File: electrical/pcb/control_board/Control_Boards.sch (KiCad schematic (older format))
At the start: 6 parts, among them M1 Mounting_Holes, y1 rover_silkscreen

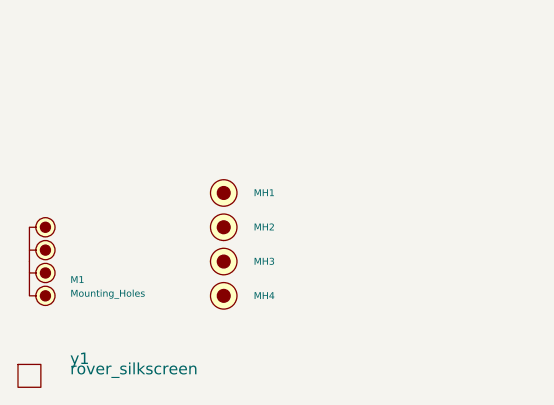
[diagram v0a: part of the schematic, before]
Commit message: moving mounting holes, unnumbering inter board connectors, and adding to kicad readme
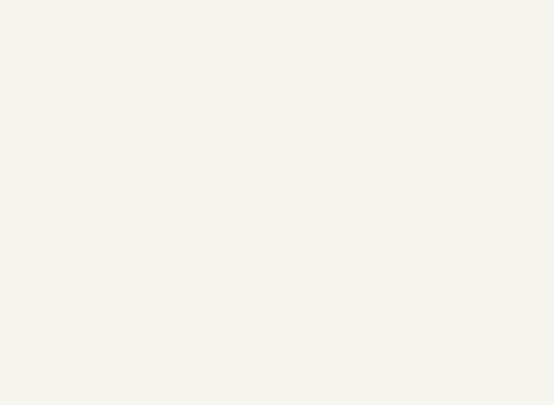
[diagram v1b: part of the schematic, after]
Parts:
- removed M1: Mounting_Holes, JPL Robotics:Raspberry pi footprint, symbol JPL_Robotics_Lib:Mounting_Holes
- removed MH1, MH2, MH3, MH4: #6THRU-HOLE, JPL Robotics:#6THRU-HOLE, symbol JPL_Robotics_Lib:#6THRU-HOLE
- removed y1: rover_silkscreen, JPL Robotics:rover_image, symbol JPL_Robotics_Lib:rover_silkscreen
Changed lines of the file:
@@
 Comment4 ""
 $EndDescr
-$Comp
-L JPL_Robotics_Lib:Mounting_Holes M1
-U 1 1 5C8D5DB2
-P 750 10200
-F 0 "M1" V 1180 10379 30  0000 L CNN
-F 1 "Mounting_Holes" V 1240 10379 30  0000 L CNN
-F 2 "JPL Robotics:Raspberry pi footprint" H 930 10380 30  0001 C CNN
-F 3 "" H 930 10380 30  0001 C CNN
-	1    750  10200
-	0    1    1    0
-$EndComp
-$Comp
-L JPL_Robotics_Lib:#6THRU-HOLE MH1
-U 1 1 5C29B1A8
-P 1600 10250
-F 0 "MH1" H 1731 10250 30  0000 L CNN
-F 1 "#6THRU-HOLE" H 1600 10390 30  0001 C CNN
-F 2 "JPL Robotics:#6THRU-HOLE" H 1600 10340 30  0001 C CNN
-F 3 "" H 1600 10340 30  0001 C CNN
-	1    1600 10250
-	1    0    0    -1
-$EndComp
-$Comp
-L JPL_Robotics_Lib:#6THRU-HOLE MH2
-U 1 1 5C29B335
-P 1600 10400
-F 0 "MH2" H 1731 10400 30  0000 L CNN
-F 1 "#6THRU-HOLE" H 1600 10540 30  0001 C CNN
-F 2 "JPL Robotics:#6THRU-HOLE" H 1600 10490 30  0001 C CNN
-F 3 "" H 1600 10490 30  0001 C CNN
-	1    1600 10400
-	1    0    0    -1
-$EndComp
-$Comp
-L JPL_Robotics_Lib:#6THRU-HOLE MH3
-U 1 1 5C2C0841
-P 1600 10550
-F 0 "MH3" H 1731 10550 30  0000 L CNN
-F 1 "#6THRU-HOLE" H 1600 10690 30  0001 C CNN
-F 2 "JPL Robotics:#6THRU-HOLE" H 1600 10640 30  0001 C CNN
-F 3 "" H 1600 10640 30  0001 C CNN
-	1    1600 10550
-	1    0    0    -1
-$EndComp
-$Comp
-L JPL_Robotics_Lib:#6THRU-HOLE MH4
-U 1 1 5C2E5D4E
-P 1600 10700
-F 0 "MH4" H 1731 10700 30  0000 L CNN
-F 1 "#6THRU-HOLE" H 1600 10840 30  0001 C CNN
-F 2 "JPL Robotics:#6THRU-HOLE" H 1600 10790 30  0001 C CNN
-F 3 "" H 1600 10790 30  0001 C CNN
-	1    1600 10700
-	1    0    0    -1
-$EndComp
-$Comp
-L JPL_Robotics_Lib:rover_silkscreen y1
-U 1 1 5D3E48F3
-P 750 11050
-F 0 "y1" H 928 11125 50  0000 L CNN
-F 1 "rover_silkscreen" H 928 11080 50  0000 L CNN
-F 2 "JPL Robotics:rover_image" H 600 11150 50  0001 C CNN
-F 3 "" H 600 11150 50  0001 C CNN
-	1    750  11050
-	1    0    0    -1
-$EndComp
 $Sheet
 S 4650 4100 3100 2350

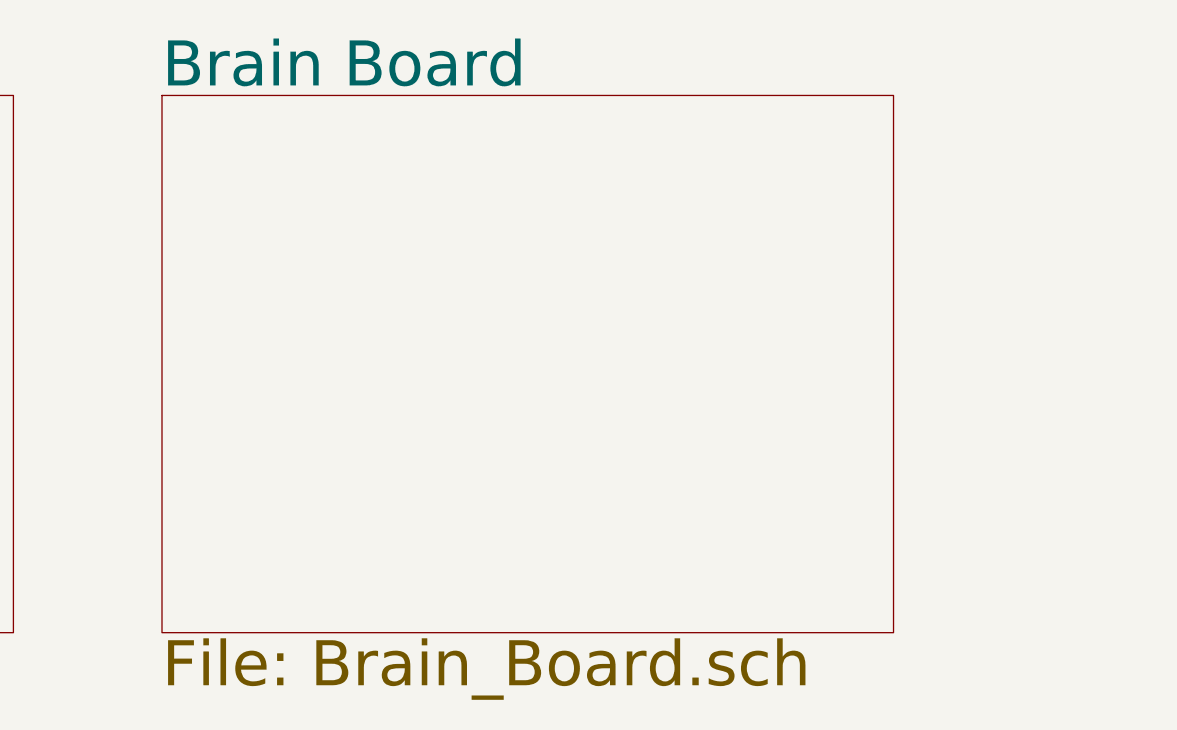
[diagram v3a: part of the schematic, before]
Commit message: Overhauled 3.3v rail and updated LEDs to use it
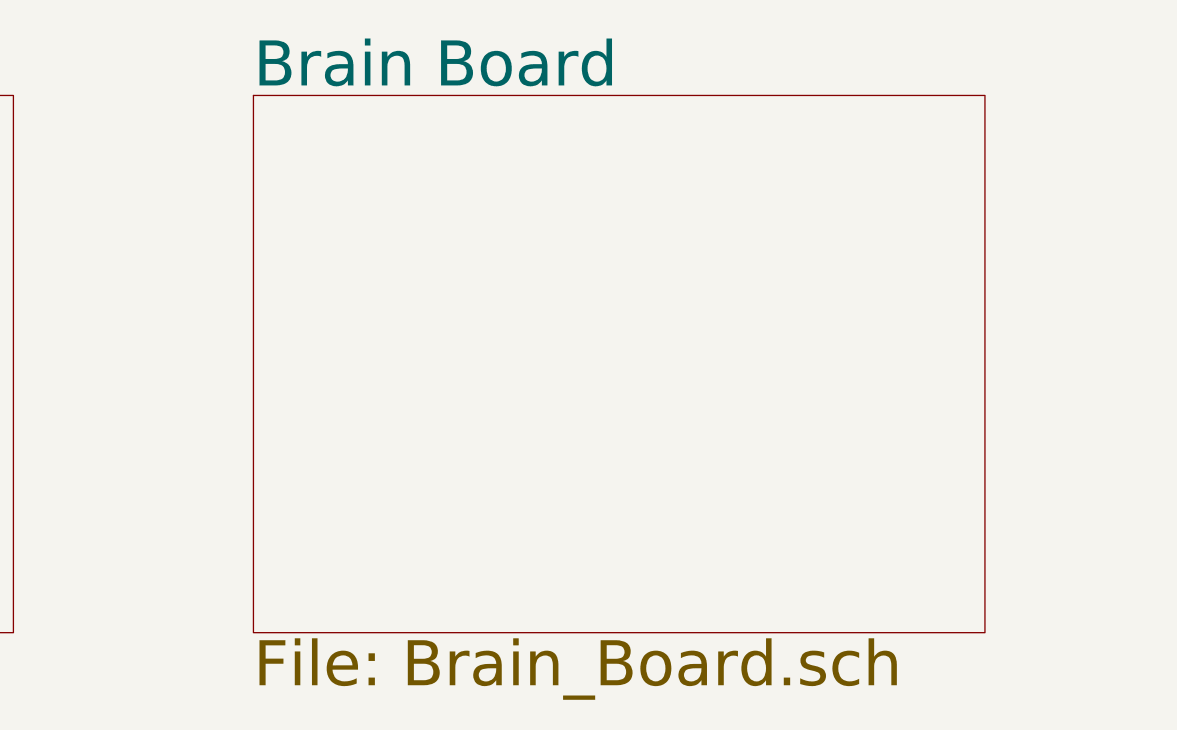
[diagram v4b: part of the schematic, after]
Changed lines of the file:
@@
 $EndSheet
 $Sheet
-S 8400 4100 3200 2350
+S 8800 4100 3200 2350
 U 60A5279E
 F0 "Brain Board" 197
